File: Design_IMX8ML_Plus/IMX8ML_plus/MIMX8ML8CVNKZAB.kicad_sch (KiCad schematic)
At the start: 2 parts, among them U1 MIMX8ML8CVNKZAB, U3 SDINBDG4-8G

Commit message: Add storage unit
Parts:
- removed unit 4 of U1
- removed U3: SDINBDG4-8G, BGA153C50P14X14_1300X1150X80N, symbol SDINBDG4-8G:SDINBDG4-8G
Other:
- added sheet storage (storage.kicad_sch)
- moved on the sheet: U1A, U1E, U1F

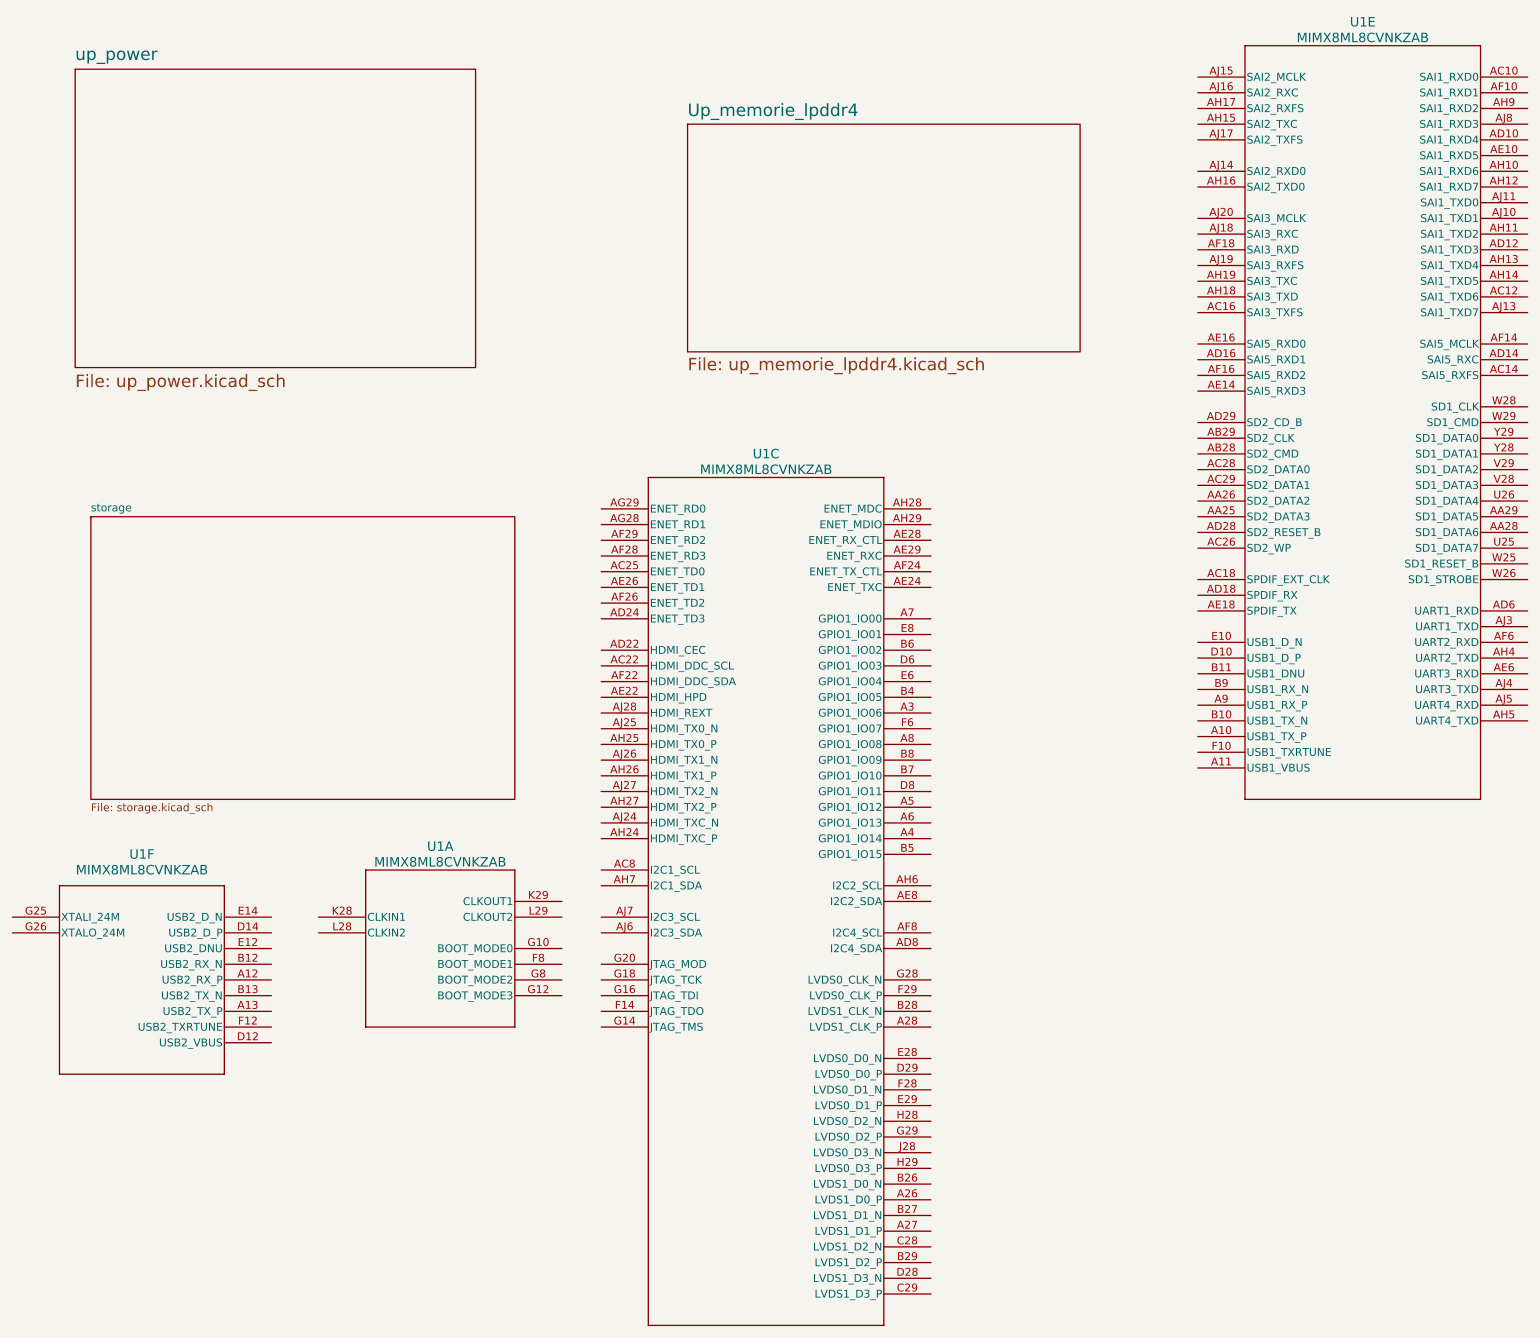
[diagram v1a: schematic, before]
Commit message: Add interface io pins
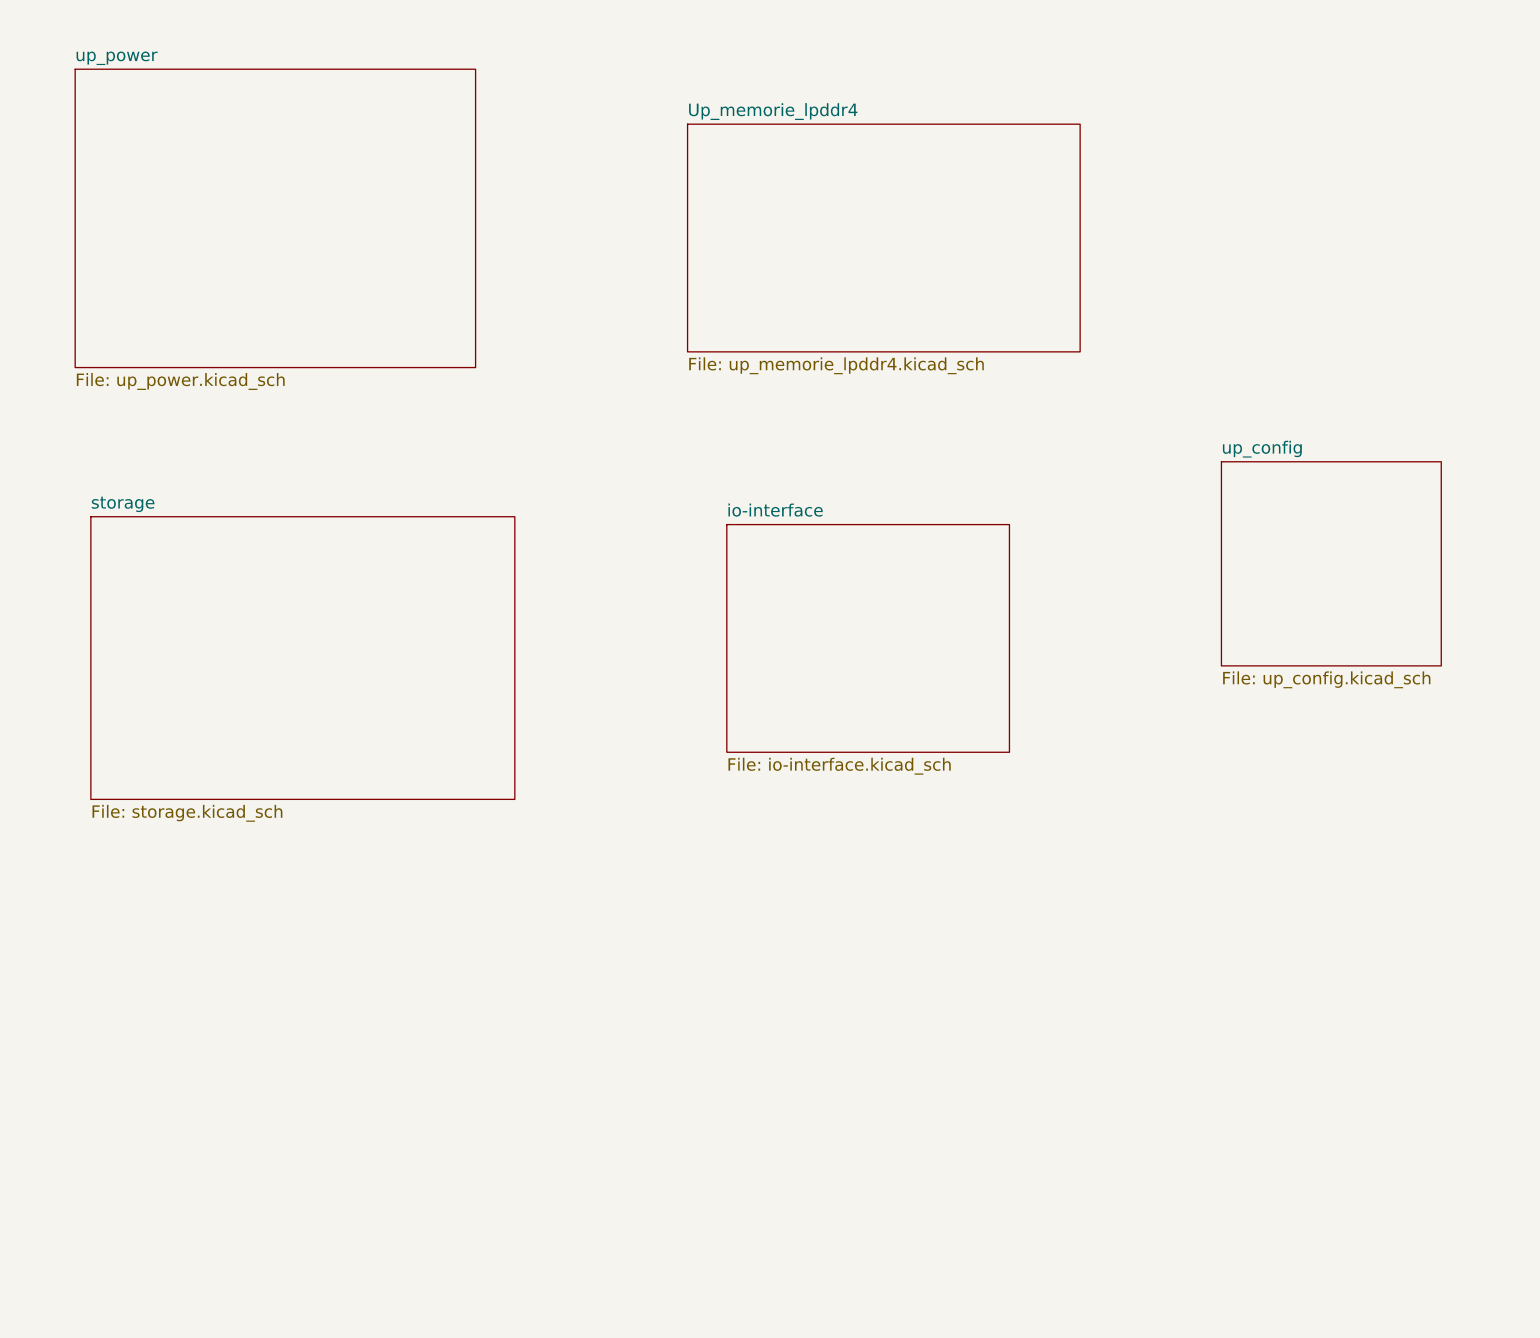
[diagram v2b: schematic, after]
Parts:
- removed U1: MIMX8ML8CVNKZAB, LFBGA548_SOT2047-1_NXP, symbol MIMX8ML8CVNKZAB:MIMX8ML8CVNKZAB
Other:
- added sheet io-interface (io-interface.kicad_sch)
- added sheet up_config (up_config.kicad_sch)

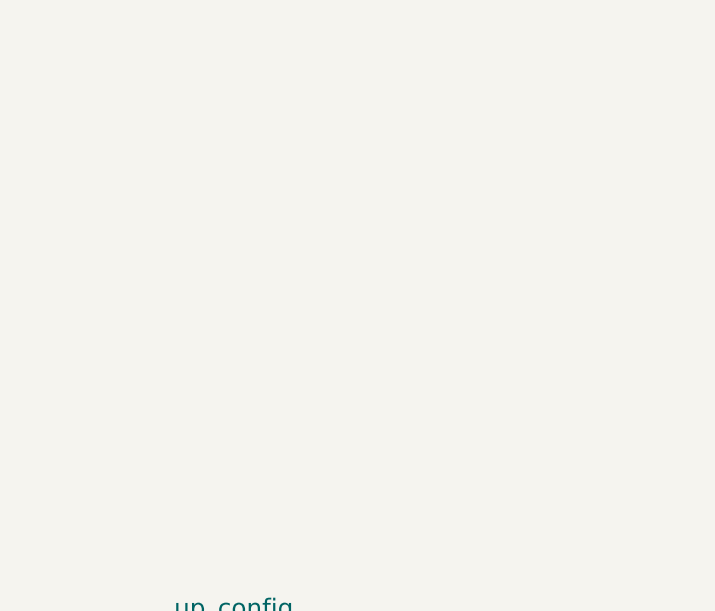
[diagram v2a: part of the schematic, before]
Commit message: Add SPB228 WIFI/BLE module
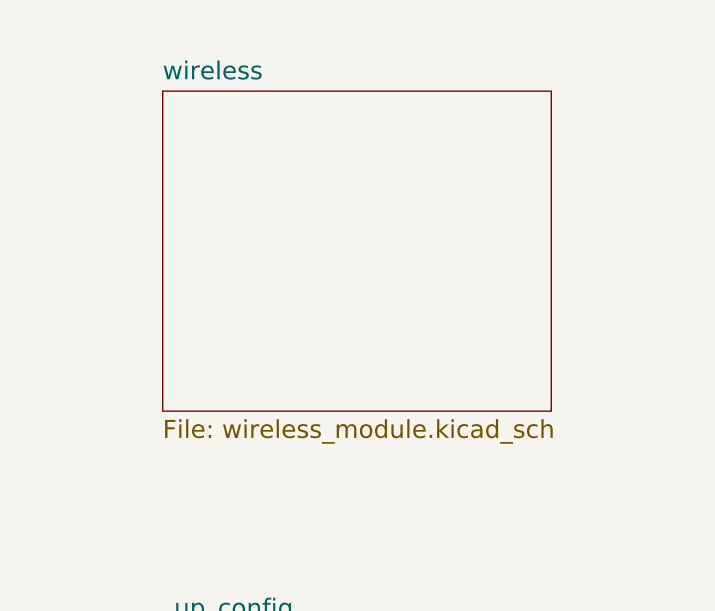
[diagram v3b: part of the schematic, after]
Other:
- added sheet wireless (wireless_module.kicad_sch)

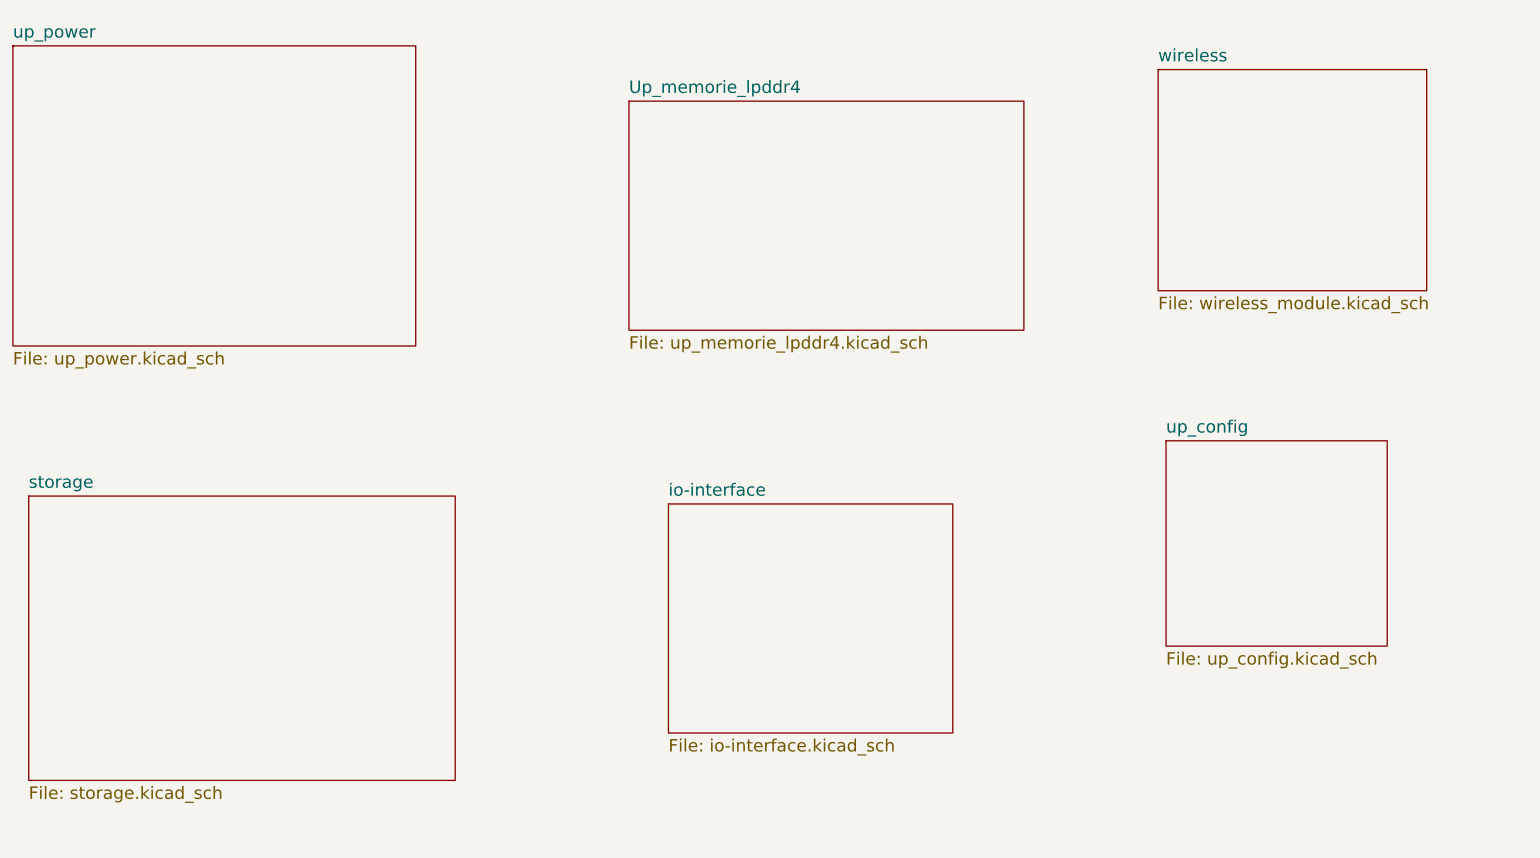
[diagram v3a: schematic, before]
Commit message: [IMX8ML-Processor] Reorganization of the pinout conector since processor to conectors
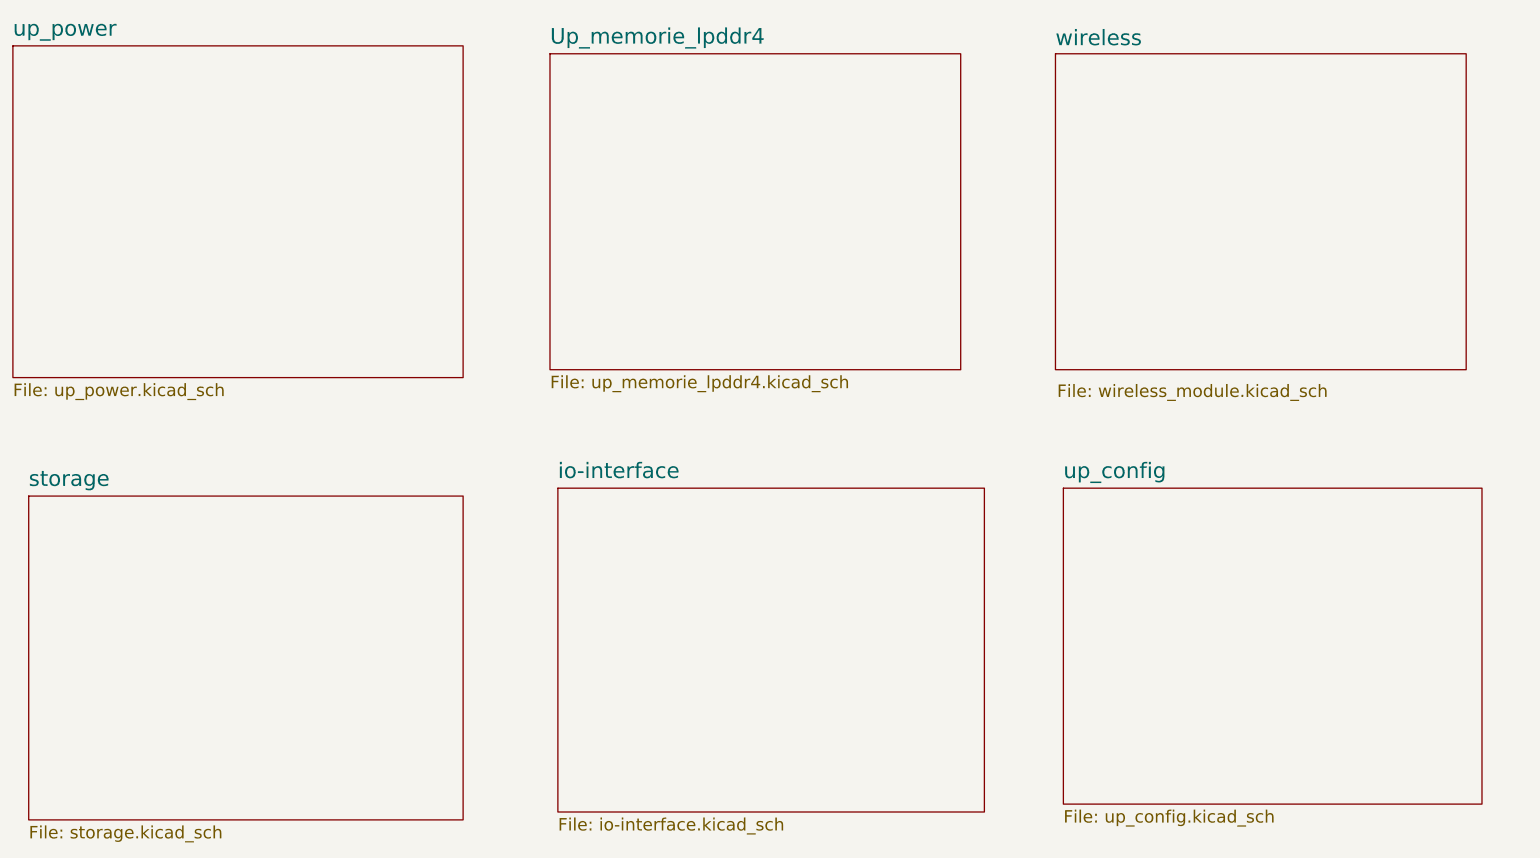
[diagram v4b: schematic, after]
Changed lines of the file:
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@@
 	(paper "A4")
 	(sheet
-		(at 133.35 39.37)
-		(size 63.5 36.83)
+		(at 120.65 31.75)
+		(size 66.04 50.8)
 		(fields_autoplaced yes)
 		(stroke
@@
 		)
 		(property "Sheetname" "Up_memorie_lpddr4"
-			(at 133.35 38.2934 0)
-			(effects
-				(font
-					(size 2 2)
+			(at 120.65 30.4234 0)
+			(effects
+				(font
+					(size 2.5 2.5)
 				)
 				(justify left bottom)
@@
 		)
 		(property "Sheetfile" "up_memorie_lpddr4.kicad_sch"
-			(at 133.35 77.0766 0)
+			(at 120.65 83.4266 0)
 			(effects
 				(font
@@
 	)
 	(sheet
-		(at 139.7 104.14)
-		(size 45.72 36.83)
+		(at 121.92 101.6)
+		(size 68.58 52.07)
 		(fields_autoplaced yes)
 		(stroke
@@
 		)
 		(property "Sheetname" "io-interface"
-			(at 139.7 103.0634 0)
-			(effects
-				(font
-					(size 2 2)
+			(at 121.92 100.2734 0)
+			(effects
+				(font
+					(size 2.5 2.5)
 				)
 				(justify left bottom)
@@
 		)
 		(property "Sheetfile" "io-interface.kicad_sch"
-			(at 139.7 141.8466 0)
+			(at 121.92 154.5466 0)
 			(effects
 				(font
@@
 	)
 	(sheet
-		(at 219.71 93.98)
-		(size 35.56 33.02)
+		(at 203.2 101.6)
+		(size 67.31 50.8)
 		(fields_autoplaced yes)
 		(stroke
@@
 		)
 		(property "Sheetname" "up_config"
-			(at 219.71 92.9034 0)
-			(effects
-				(font
-					(size 2 2)
+			(at 203.2 100.2734 0)
+			(effects
+				(font
+					(size 2.5 2.5)
 				)
 				(justify left bottom)
@@
 		)
 		(property "Sheetfile" "up_config.kicad_sch"
-			(at 219.71 127.8766 0)
+			(at 203.2 153.2766 0)
 			(effects
 				(font
@@
 	)
 	(sheet
-		(at 218.44 34.29)
-		(size 43.18 35.56)
-		(fields_autoplaced yes)
+		(at 201.93 31.75)
+		(size 66.04 50.8)
 		(stroke
 			(width 0.1524)
@@
 		)
 		(property "Sheetname" "wireless"
-			(at 218.44 33.2134 0)
-			(effects
-				(font
-					(size 2 2)
+			(at 201.93 30.6734 0)
+			(effects
+				(font
+					(size 2.5 2.5)
 				)
 				(justify left bottom)
@@
 		)
 		(property "Sheetfile" "wireless_module.kicad_sch"
-			(at 218.44 70.7266 0)
+			(at 202.184 84.836 0)
 			(effects
 				(font
@@
 	(sheet
 		(at 36.83 102.87)
-		(size 68.58 45.72)
+		(size 69.85 52.07)
 		(fields_autoplaced yes)
 		(stroke
@@
 		)
 		(property "Sheetname" "storage"
-			(at 36.83 101.7934 0)
-			(effects
-				(font
-					(size 2 2)
+			(at 36.83 101.5434 0)
+			(effects
+				(font
+					(size 2.5 2.5)
 				)
 				(justify left bottom)
@@
 		)
 		(property "Sheetfile" "storage.kicad_sch"
-			(at 36.83 149.4666 0)
+			(at 36.83 155.8166 0)
 			(effects
 				(font
@@
 	(sheet
 		(at 34.29 30.48)
-		(size 64.77 48.26)
+		(size 72.39 53.34)
 		(fields_autoplaced yes)
 		(stroke
@@
 		)
 		(property "Sheetname" "up_power"
-			(at 34.29 29.4034 0)
-			(effects
-				(font
-					(size 2 2)
+			(at 34.29 29.1534 0)
+			(effects
+				(font
+					(size 2.5 2.5)
 				)
 				(justify left bottom)
@@
 		)
 		(property "Sheetfile" "up_power.kicad_sch"
-			(at 34.29 79.6166 0)
-			(effects
-				(font
+			(at 34.29 84.6966 0)
+			(effects
+				(font
